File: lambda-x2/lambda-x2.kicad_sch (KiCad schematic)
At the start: 129 parts, among them J1 FTSH-107-01-F-DV-K, J3 Conn_02x02_Odd_Even, J4 Conn_01x10, P1 33311-24AW-2, Q1 BTS3028, Q2 BTS3028, Q3 BTS3028, Q4 BTS3028, U17 MCP6002T-I/SN, U18 JDY-33, U2 STM32F103C6Tx, U4 LM78M05_TO252, U5 XC6206P332MR, U6 REF3033, U7 MCP6002T-I/SN, U8 TJA1051T-3, Y1 XXDCELNANF-8MHZ

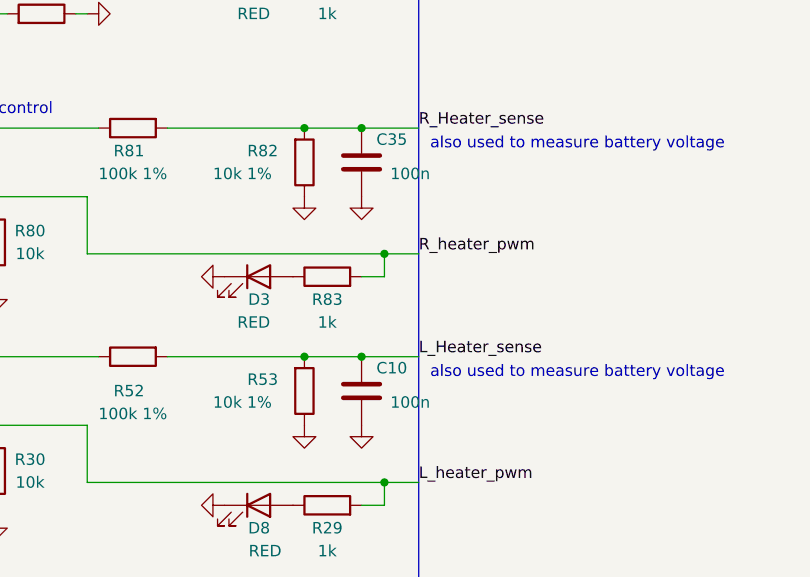
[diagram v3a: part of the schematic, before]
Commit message: lambda-x2: fix RC filter values on heater voltage ADC inputs
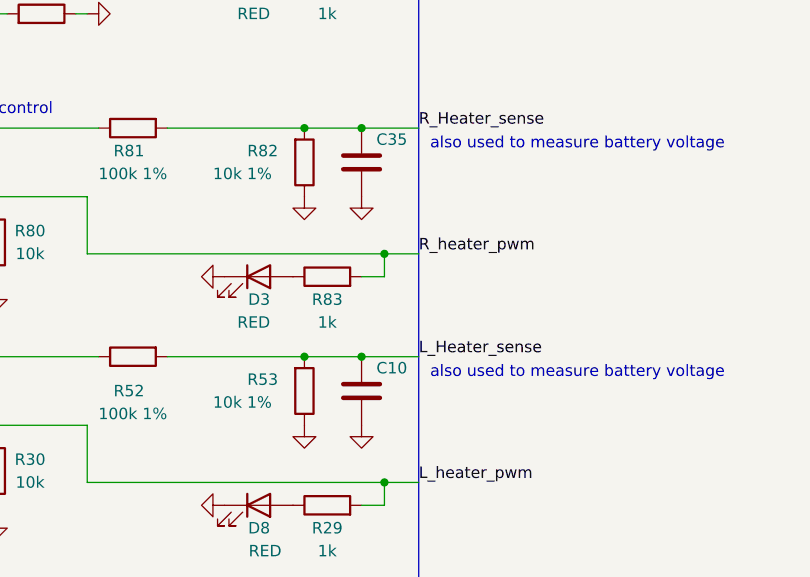
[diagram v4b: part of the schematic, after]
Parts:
- C10, C35: value 100n -> (none); footprint Capacitor_SMD:C_0402_1005Metric -> (none); LCSC C1525 -> C106205
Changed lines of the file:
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@@
       (effects (font (size 1.27 1.27)) (justify left))
     )
-    (property "Value" "100n" (id 1) (at 236.22 251.46 0)
-      (effects (font (size 1.27 1.27)) (justify left))
-    )
-    (property "Footprint" "Capacitor_SMD:C_0402_1005Metric" (id 2) (at 227.6348 254 0)
+    (property "Value" "" (id 1) (at 236.22 251.46 0)
+      (effects (font (size 1.27 1.27)) (justify left))
+    )
+    (property "Footprint" "" (id 2) (at 227.6348 254 0)
       (effects (font (size 1.27 1.27)) hide)
     )
@@
       (effects (font (size 1.27 1.27)) hide)
     )
-    (property "LCSC" "C1525" (id 4) (at 228.6 250.19 0)
+    (property "LCSC" "C106205" (id 4) (at 228.6 250.19 0)
       (effects (font (size 1.27 1.27)) hide)
     )
@@
       (effects (font (size 1.27 1.27)) (justify left))
     )
-    (property "Value" "100n" (id 1) (at 236.22 226.06 0)
-      (effects (font (size 1.27 1.27)) (justify left))
-    )
-    (property "Footprint" "Capacitor_SMD:C_0402_1005Metric" (id 2) (at 227.6348 228.6 0)
+    (property "Value" "" (id 1) (at 236.22 226.06 0)
+      (effects (font (size 1.27 1.27)) (justify left))
+    )
+    (property "Footprint" "" (id 2) (at 227.6348 228.6 0)
       (effects (font (size 1.27 1.27)) hide)
     )
@@
       (effects (font (size 1.27 1.27)) hide)
     )
-    (property "LCSC" "C1525" (id 4) (at 228.6 224.79 0)
+    (property "LCSC" "C106205" (id 4) (at 228.6 224.79 0)
       (effects (font (size 1.27 1.27)) hide)
     )
@@
     )
     (path "/7e9bb2b4-4718-4b7a-89b2-88a429383acd"
-      (reference "C10") (unit 1) (value "100n") (footprint "Capacitor_SMD:C_0402_1005Metric")
+      (reference "C10") (unit 1) (value "1n") (footprint "Capacitor_SMD:C_0402_1005Metric")
     )
     (path "/1eda4d5a-8f94-40d8-8cab-d6c152c81f10/d6412550-43c8-4f65-9cde-891803e0dfc5"
@@
     )
     (path "/dd2b7db6-de75-4188-8d2d-42b620017345"
-      (reference "C35") (unit 1) (value "100n") (footprint "Capacitor_SMD:C_0402_1005Metric")
+      (reference "C35") (unit 1) (value "1n") (footprint "Capacitor_SMD:C_0402_1005Metric")
     )
     (path "/00000000-0000-0000-0000-00006000572f"

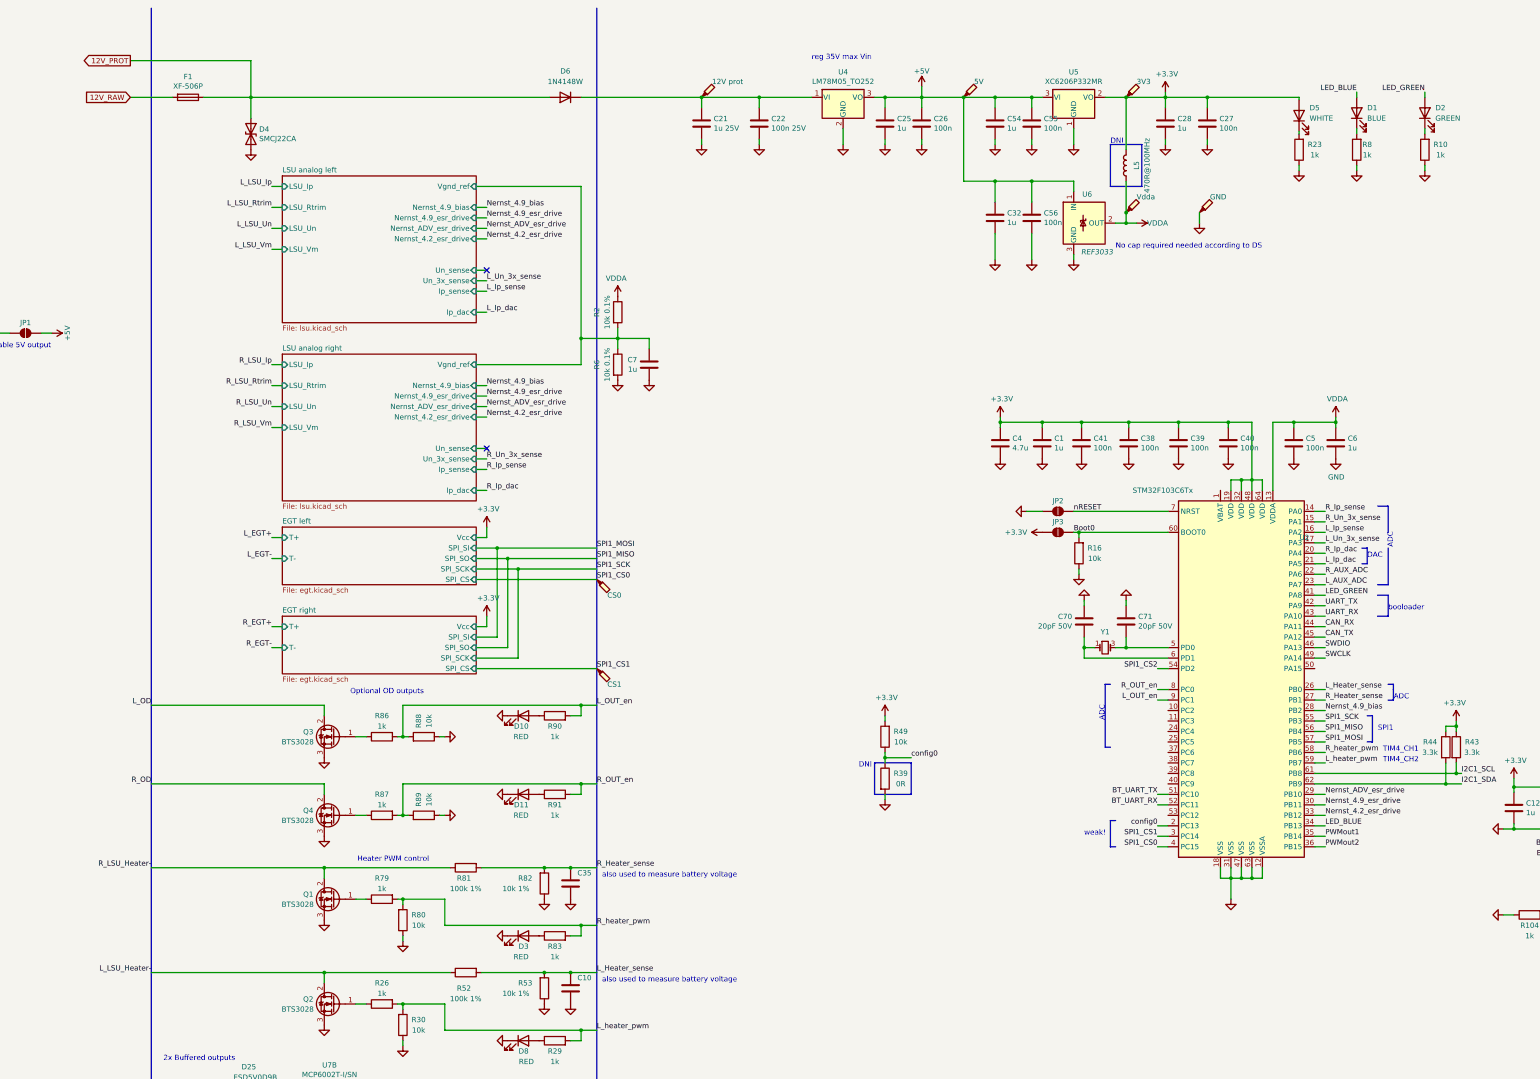
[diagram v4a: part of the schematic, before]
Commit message: lambda-x2: fuse, Vbat sense, resistor in sense
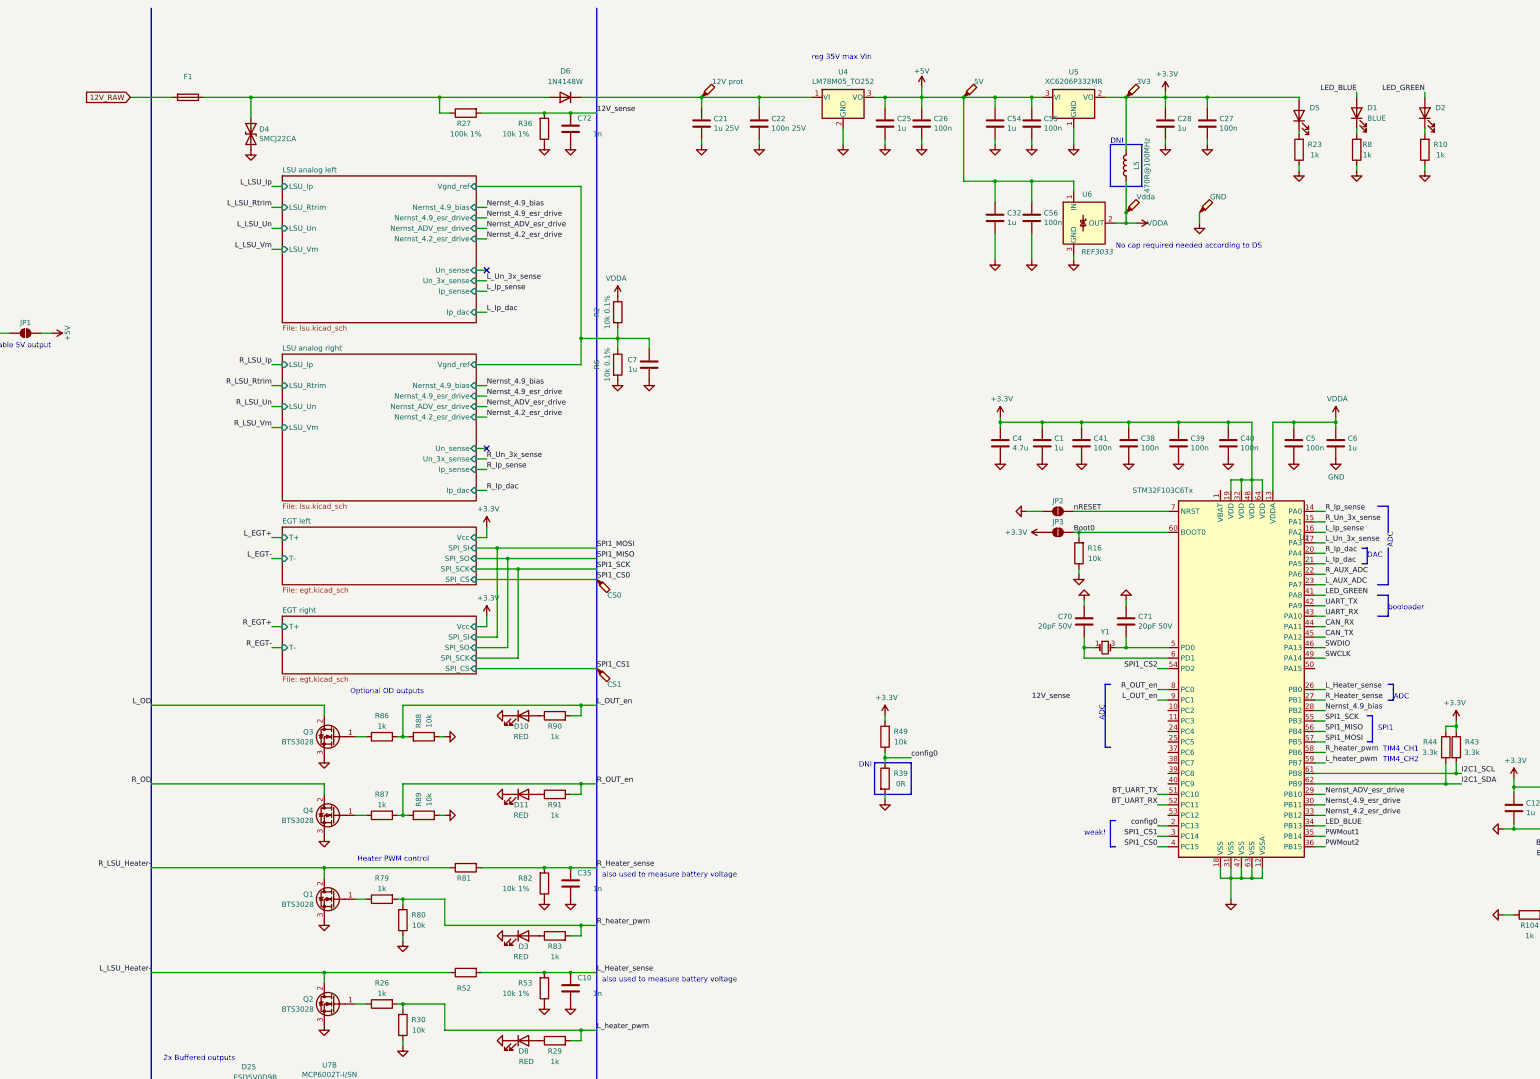
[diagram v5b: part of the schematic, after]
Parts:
- added C72: 1n, Capacitor_SMD:C_0402_1005Metric, symbol Device:C
- added R27: 100k 1%, Resistor_SMD:R_0603_1608Metric, symbol Device:R
- added R36: 10k 1%, Resistor_SMD:R_0402_1005Metric, symbol Device:R
- C10, C35: value (none) -> 1n; footprint (none) -> Capacitor_SMD:C_0402_1005Metric
- D2: value GREEN -> (none); footprint LED_SMD:LED_0603_1608Metric -> (none)
- D5: value WHITE -> (none); footprint LED_SMD:LED_0603_1608Metric -> (none); LCSC C2290 -> C72043
- F1: value XF-506P -> (none); footprint wideband_controller:XF-506P -> (none); LCSC C492610 -> C2977524
- R52, R81: value 100k 1% -> (none); footprint Resistor_SMD:R_0402_1005Metric -> (none); LCSC C25741 -> C217279
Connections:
- net GND: now also C72.2, R36.1
- net 12V_PROT: no longer names the net of D4.1 (A1), D6.2 (A), F1.1
- net 12V_PROT: now also R27.1
- new net 12V_sense: C72.1, R27.2, R36.2

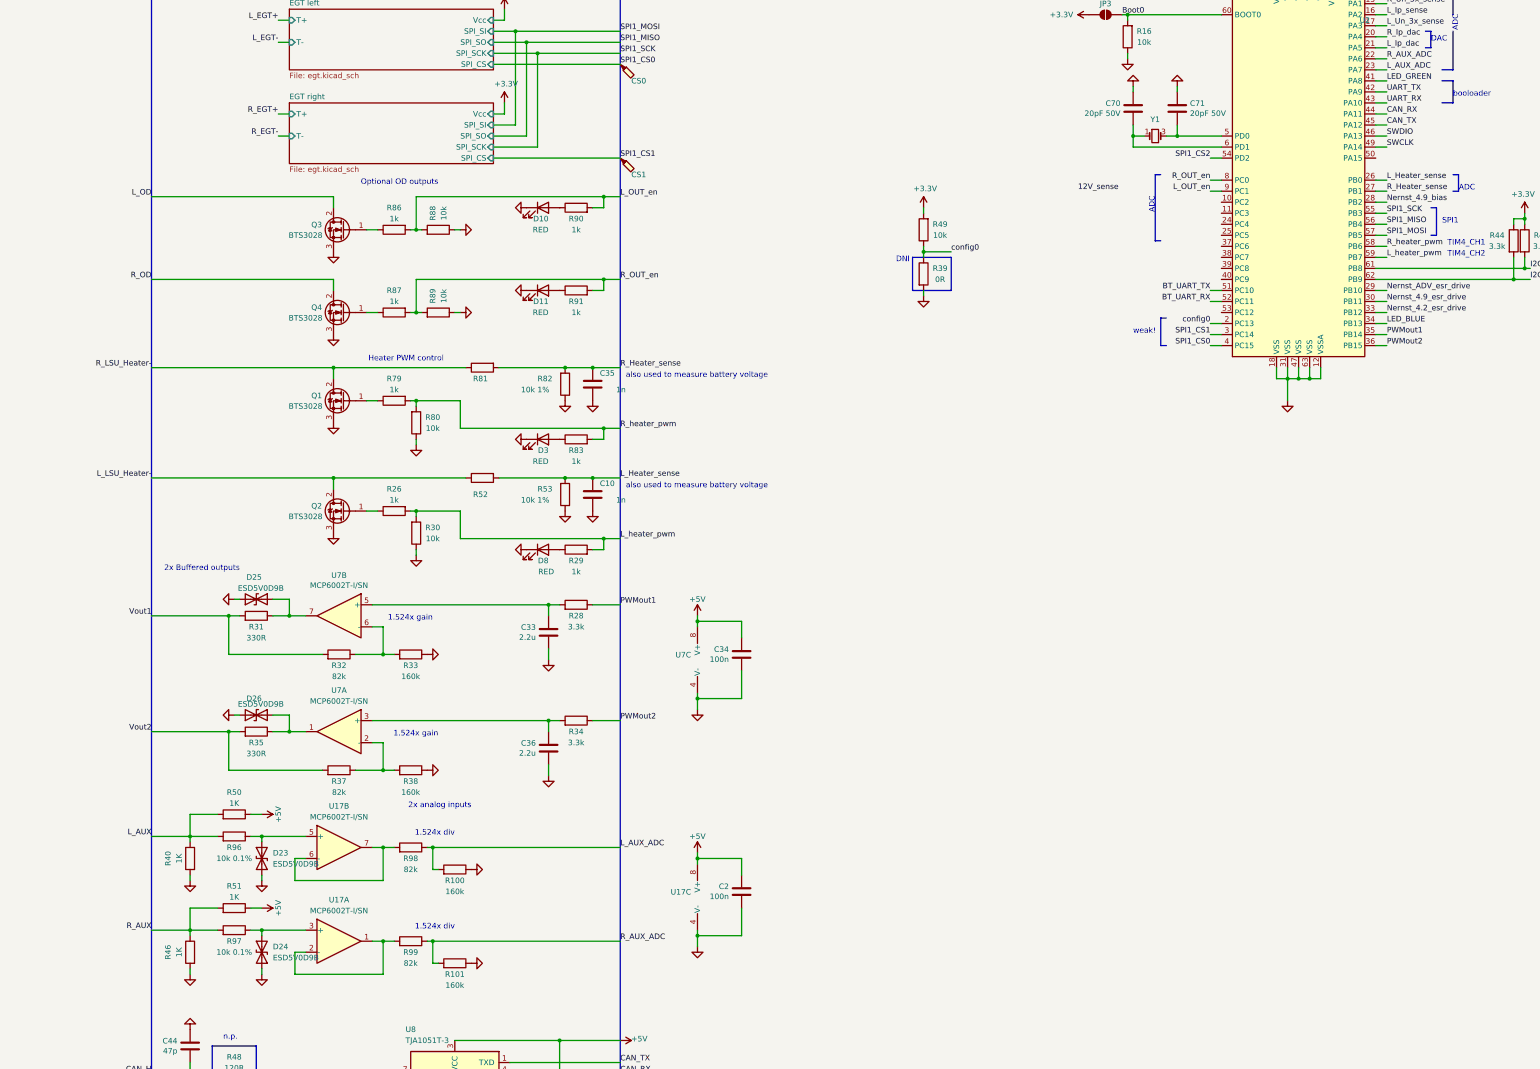
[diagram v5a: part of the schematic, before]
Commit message: lambda-x2: diagnostic for AUX out, PWM noise cancelation, etc
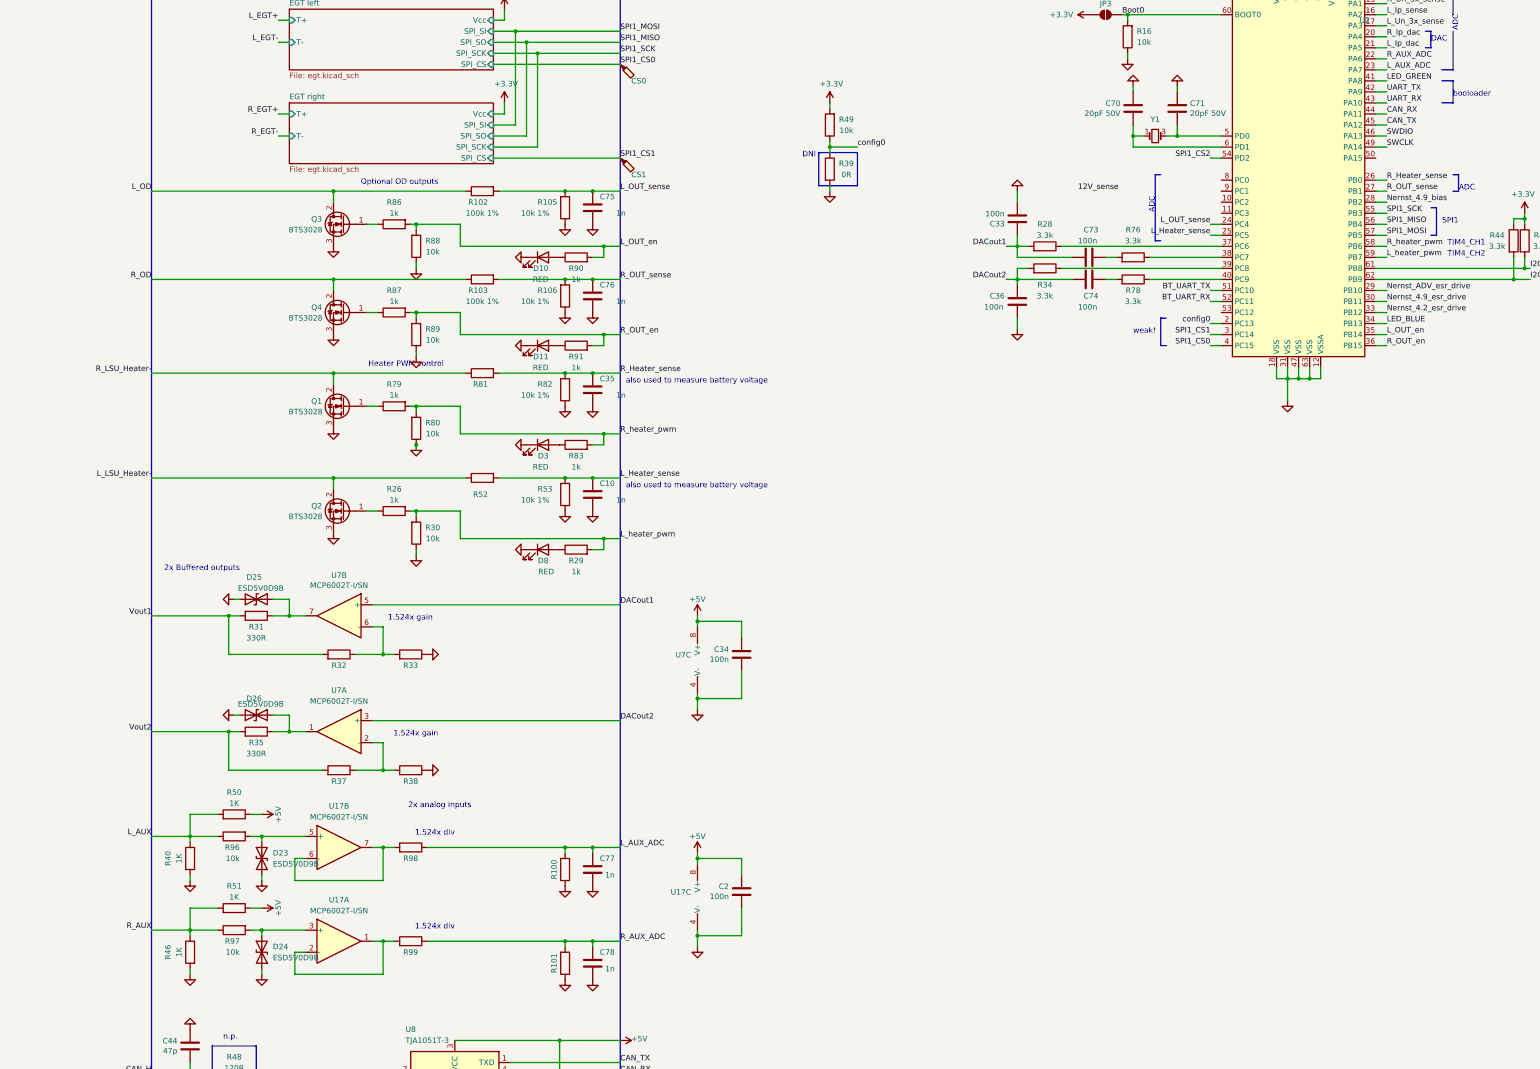
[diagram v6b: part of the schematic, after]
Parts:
- added C73, C74: 100n, Capacitor_SMD:C_0402_1005Metric, symbol Device:C
- added C75, C76, C77, C78: 1n, Capacitor_SMD:C_0402_1005Metric, symbol Device:C
- added R102, R103: 100k 1%, Resistor_SMD:R_0603_1608Metric, symbol Device:R
- added R105, R106: 10k 1%, Resistor_SMD:R_0402_1005Metric, symbol Device:R
- added R76, R78: 3.3k, Resistor_SMD:R_0402_1005Metric, symbol Device:R
- C33, C36: value 2.2u -> 100n; LCSC C12530 -> C1525
- R100, R101, R33, R38: value 160k -> (none); footprint Resistor_SMD:R_0603_1608Metric -> (none); LCSC C22813 -> C409854
- R32, R98, R99: value 82k -> (none); footprint Resistor_SMD:R_0603_1608Metric -> (none); LCSC C23254 -> C325373
- R37: value 82k -> (none); footprint Resistor_SMD:R_0603_1608Metric -> (none)
- R96, R97: value 10k 0.1% -> 10k; footprint Resistor_SMD:R_0603_1608Metric -> Resistor_SMD:R_0402_1005Metric; LCSC C309083 -> C25744
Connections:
- net GND: now also C75.2, C76.2, C77.2, C78.2, R105.1, R106.1
- net L_AUX: now also R96.1; no longer R96.2
- net L_AUX_ADC: now also C77.1
- net L_Heater_sense: now also U2.25 (PC5); no longer U2.26 (PB0)
- net L_OD: now also R102.1
- net L_OUT_en: now also U2.35 (PB14); no longer U2.9 (PC1)
- net R_AUX: now also R97.1; no longer R97.2
- net R_AUX_ADC: now also C78.1
- net R_Heater_sense: now also U2.26 (PB0); no longer U2.27 (PB1)
- net R_OD: now also R103.1
- net R_OUT_en: now also U2.36 (PB15); no longer U2.8 (PC0)
- net DACout2: now reaches C36.1, R34.2, U7.3 (+)
- net DACout2: now also C74.2
- net DACout1: now reaches C33.1, R28.2, U7.5 (+)
- net DACout1: now also C73.2
- net at D23.1 (A1), U17.5 (+): now also R96.2; no longer R96.1
- net at D24.1 (A1), U17.3 (+): now also R97.2; no longer R97.1
- net L_OUT_sense: now reaches U2.24 (PC4)
- net L_OUT_sense: now also C75.1, R102.2, R105.2
- net at U2.37 (PC6): now also R28.1
- net at U2.38 (PC7): now also R76.1
- net at U2.39 (PC8): now also R34.1
- net at U2.40 (PC9): now also R78.1
- removed net PWMout1: R28.1, U2.35 (PB14)
- removed net PWMout2: R34.1, U2.36 (PB15)
- new net: C74.1, R78.2
- new net: C73.1, R76.2
- new net R_OUT_sense: C76.1, R103.2, R106.2, U2.27 (PB1)
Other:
- moved on the sheet: C35, D10, D11, D3, Q1, Q3, R100, R101, R28, R34, R39, R49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

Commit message: lambda-x2: jtag, adc channels, one more led, BT en, etc
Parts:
- added C79, C80: 1n, Capacitor_SMD:C_0402_1005Metric, symbol Device:C
- added D30: GREEN, LED_SMD:LED_0603_1608Metric, symbol Device:LED
- added J2: (no value), symbol wideband_controller-cache:tc2030-idc-nl
- added R109, R110, R111: 1k, Resistor_SMD:R_0402_1005Metric, symbol Device:R
- D2, D5: value (none) -> GREEN; footprint (none) -> LED_SMD:LED_0603_1608Metric
- F1: value (none) -> BSMD1206-025-33V; footprint (none) -> Fuse:Fuse_1206_3216Metric
- R100, R101, R33, R38: value (none) -> 160k; footprint (none) -> Resistor_SMD:R_0402_1005Metric
- R32, R37, R98, R99: value (none) -> 82k; footprint (none) -> Resistor_SMD:R_0402_1005Metric
- R52, R81: value (none) -> 100k 1%; footprint (none) -> Resistor_SMD:R_0603_1608Metric
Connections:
- net +3V3: now also J2.1 (VCC)
- net 12V_sense: now also U2.8 (PC0)
- net GND: now also C79.2, C80.2, J2.5 (GND), R111.1
- net LSU analog left/Un_sense: now also R109.1
- net LSU analog right/Un_sense: now also R110.1
- net L_Ip_sense: now also U2.11 (PC3); no longer U2.16 (PA2)
- net L_Un_3x_sense: now also U2.10 (PC2); no longer U2.17 (PA3)
- net SWCLK: now also J2.4 (SWCLK)
- net SWDIO: now also J2.2 (SWDIO)
- net nRESET: now also J2.3 (NRESET)
- net BT_EN: now reaches U18.15 (EN)
- net BT_EN: now also U2.50 (PA15)
- net R_LED_GREEN: now reaches U2.9 (PC1)
- net R_LED_GREEN: now also D30.2 (A)
- net LED_GREEN renamed L_LED_GREEN
- new net: D30.1 (K), R111.2
- new net L_Un_sense: C79.1, R109.2, U2.17 (PA3)
- new net R_Un_sense: C80.1, R110.2, U2.16 (PA2)
- new net SWO: J2.6 (SWO)
- no-connect marks 7 -> 5
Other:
- moved on the sheet: C7, R2, R6
